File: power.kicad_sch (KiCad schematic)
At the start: 28 parts, among them U12 TPS54302, U2 SCT2450

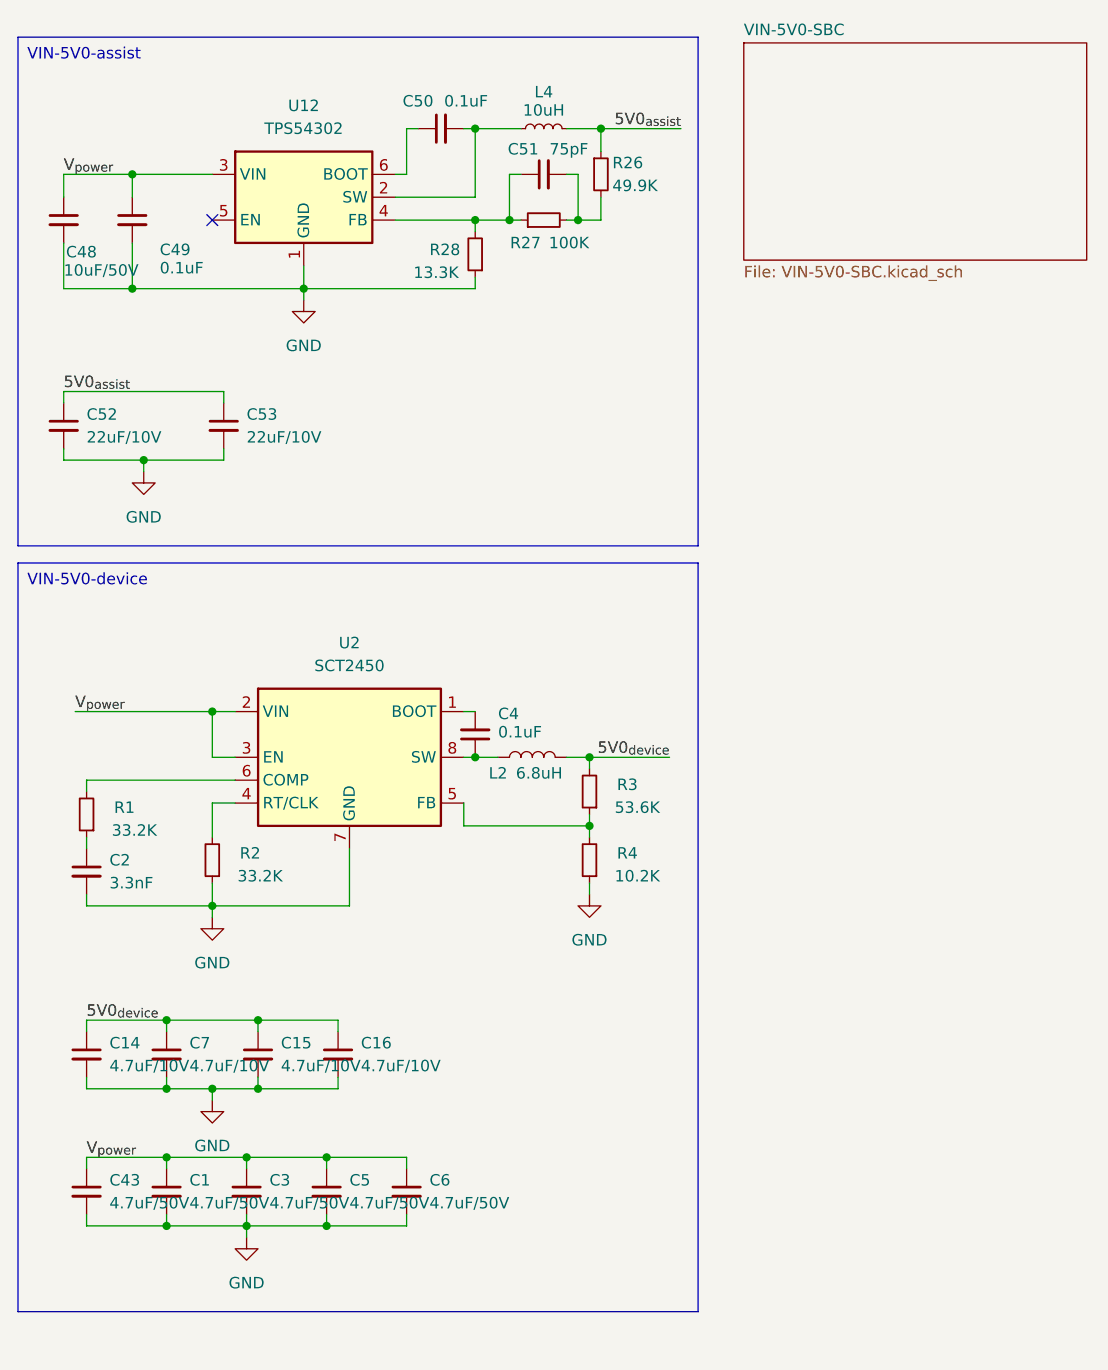
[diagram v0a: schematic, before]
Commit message: 暂存: 基本完成原理图(未分配封装，未ERC)
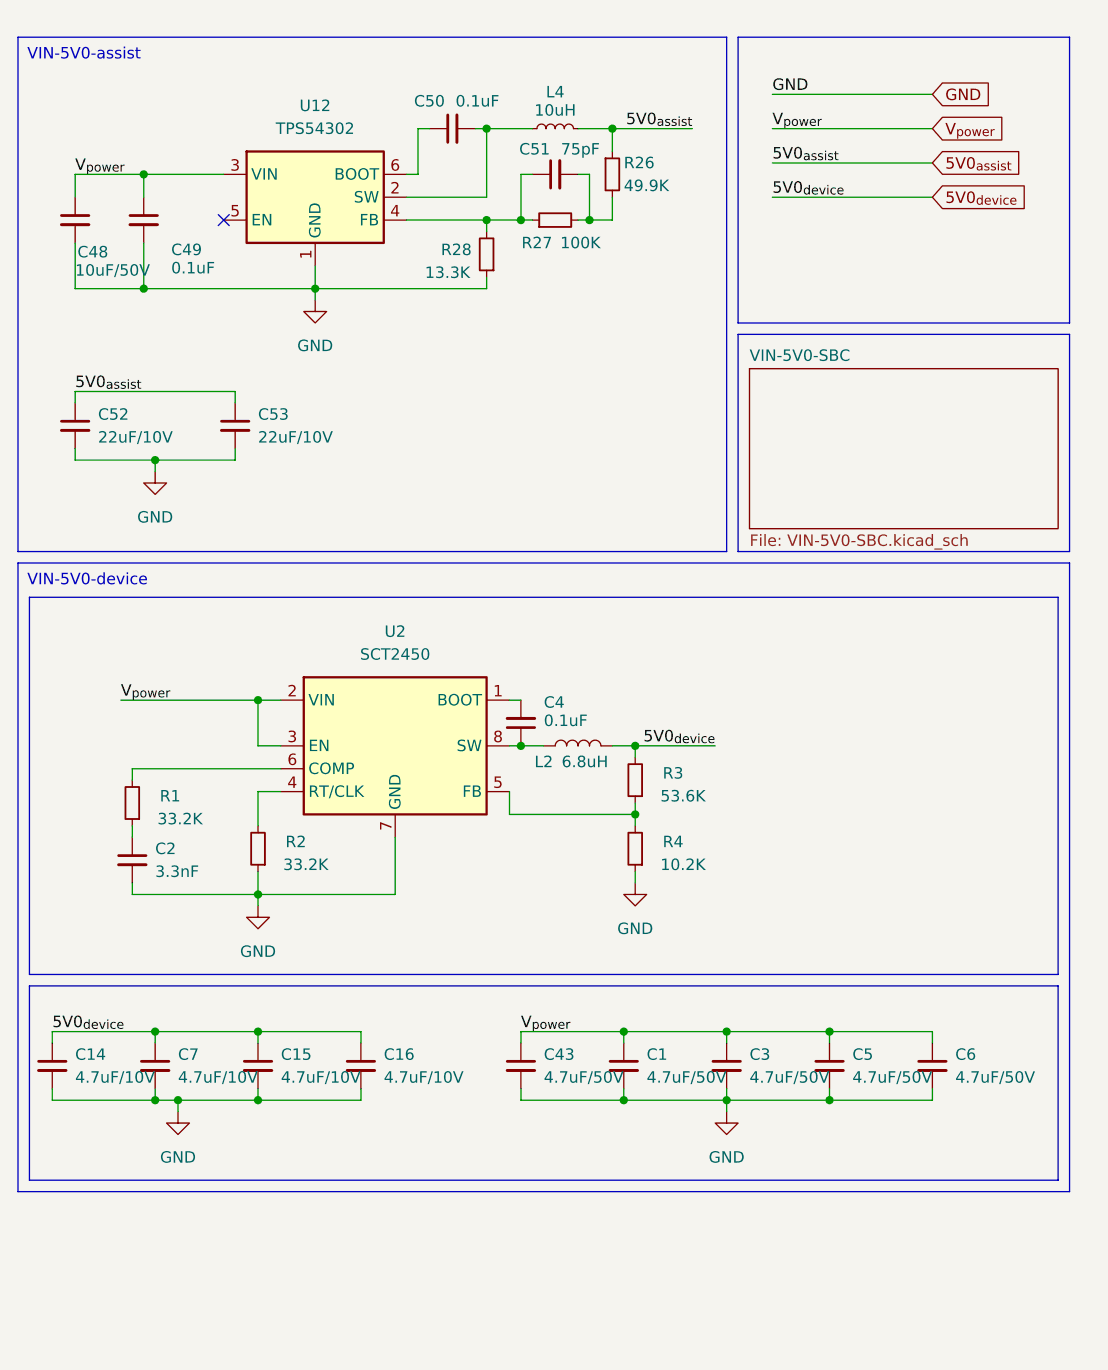
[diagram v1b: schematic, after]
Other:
- moved on the sheet: C1, C14, C15, C16, C2, C3, C4, C43, C48, C49, C5, C50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

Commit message: 暂存: 基本完成原理图(差雷达接口)
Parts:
- C12: renamed from C14; footprint (none) -> Capacitor_SMD:C_0603_1608Metric
- C13: renamed from C48; footprint (none) -> Capacitor_SMD:C_1206_3216Metric
- C14: renamed from C52; footprint (none) -> Capacitor_SMD:C_1206_3216Metric
- C15: renamed from C2; footprint (none) -> Capacitor_SMD:C_0402_1005Metric
- C16: renamed from C49; footprint (none) -> Capacitor_SMD:C_0402_1005Metric
- C17: renamed from C7; footprint (none) -> Capacitor_SMD:C_0603_1608Metric
- C18: renamed from C53; footprint (none) -> Capacitor_SMD:C_1206_3216Metric
- C19: renamed from C15; footprint (none) -> Capacitor_SMD:C_0603_1608Metric
- C20: renamed from C16; footprint (none) -> Capacitor_SMD:C_0603_1608Metric
- C21: renamed from C50; footprint (none) -> Capacitor_SMD:C_0402_1005Metric
- C22: renamed from C4; footprint (none) -> Capacitor_SMD:C_0402_1005Metric
- C23: renamed from C43; footprint (none) -> Capacitor_SMD:C_0805_2012Metric
- C24: renamed from C51; footprint (none) -> Capacitor_SMD:C_0402_1005Metric
- C25: renamed from C1; footprint (none) -> Capacitor_SMD:C_0805_2012Metric
- C26: renamed from C3; footprint (none) -> Capacitor_SMD:C_0805_2012Metric
- C27: renamed from C5; footprint (none) -> Capacitor_SMD:C_0805_2012Metric
- C28: renamed from C6; footprint (none) -> Capacitor_SMD:C_0805_2012Metric
- L1: renamed from L4; footprint (none) -> Inductor_SMD:L_APV_APH0530
- L2: footprint (none) -> Inductor_SMD:L_APV_APH0630
- R10: renamed from R27; footprint (none) -> Resistor_SMD:R_0402_1005Metric
- R11: renamed from R26; footprint (none) -> Resistor_SMD:R_0603_1608Metric
- R12: renamed from R3; footprint (none) -> Resistor_SMD:R_0603_1608Metric
- R13: renamed from R4; footprint (none) -> Resistor_SMD:R_0603_1608Metric
- R7: renamed from R1; footprint (none) -> Resistor_SMD:R_0603_1608Metric
- R8: renamed from R2; value 33.2K -> 200K; footprint (none) -> Resistor_SMD:R_0402_1005Metric
- R9: renamed from R28; footprint (none) -> Resistor_SMD:R_0603_1608Metric
- U5: renamed from U2; footprint (none) -> Package_SO:HSOP-8-1EP_3.9x4.9mm_P1.27mm_EP2.3x2.3mm
- renumbered U12 to U4

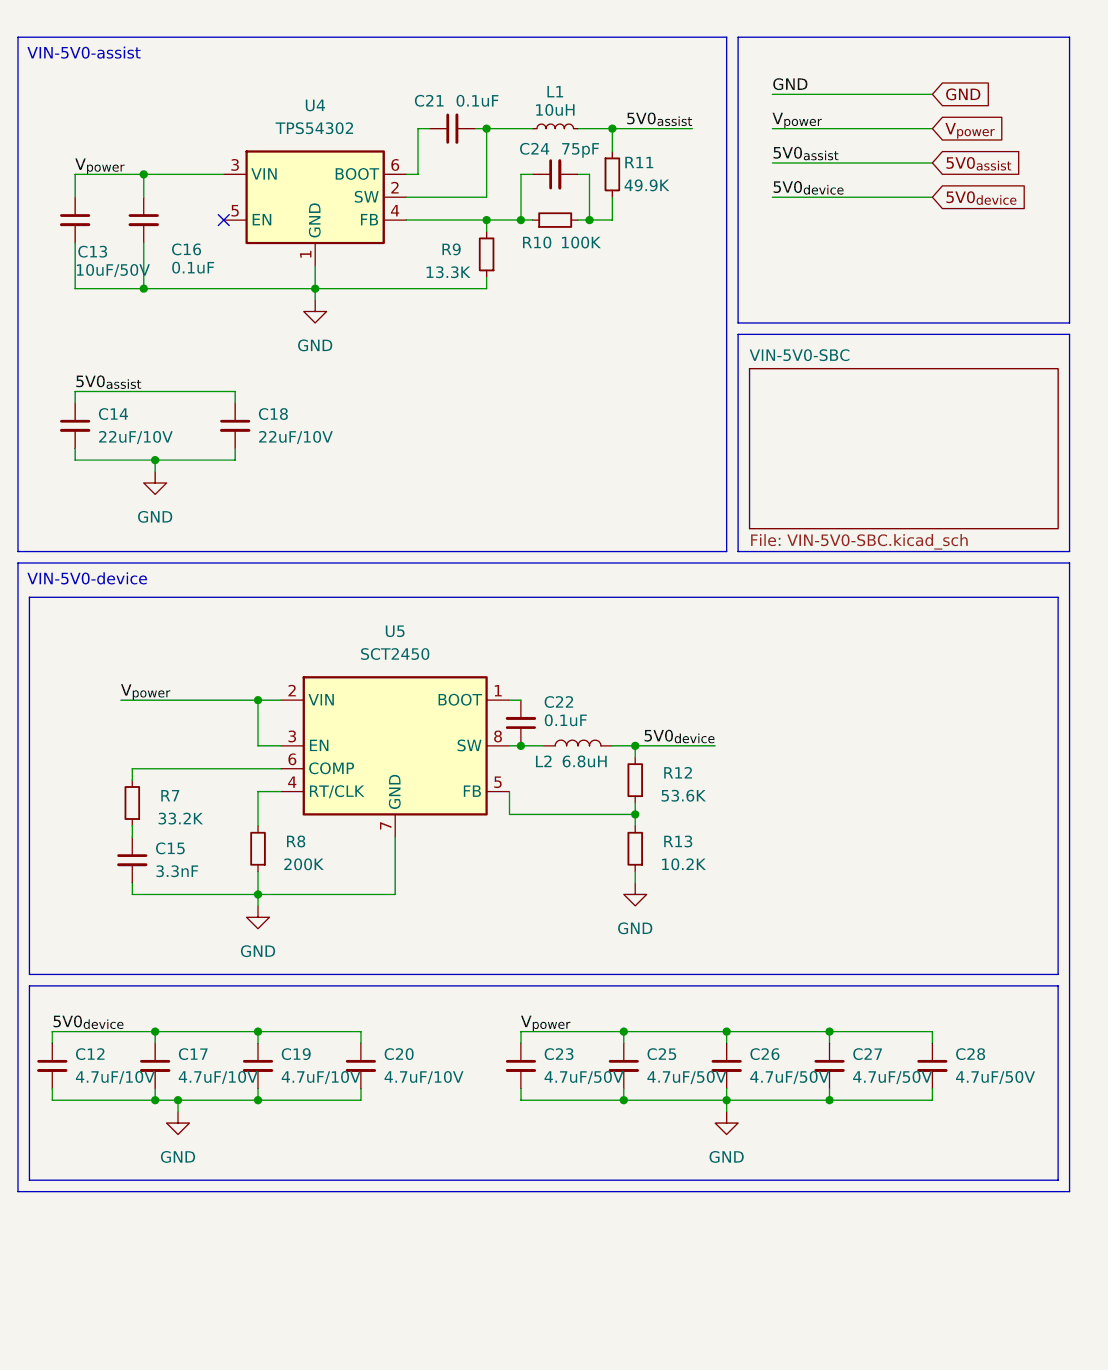
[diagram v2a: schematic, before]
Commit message: 暂存: 布局布线基本完成(DRC未过，GND不全)
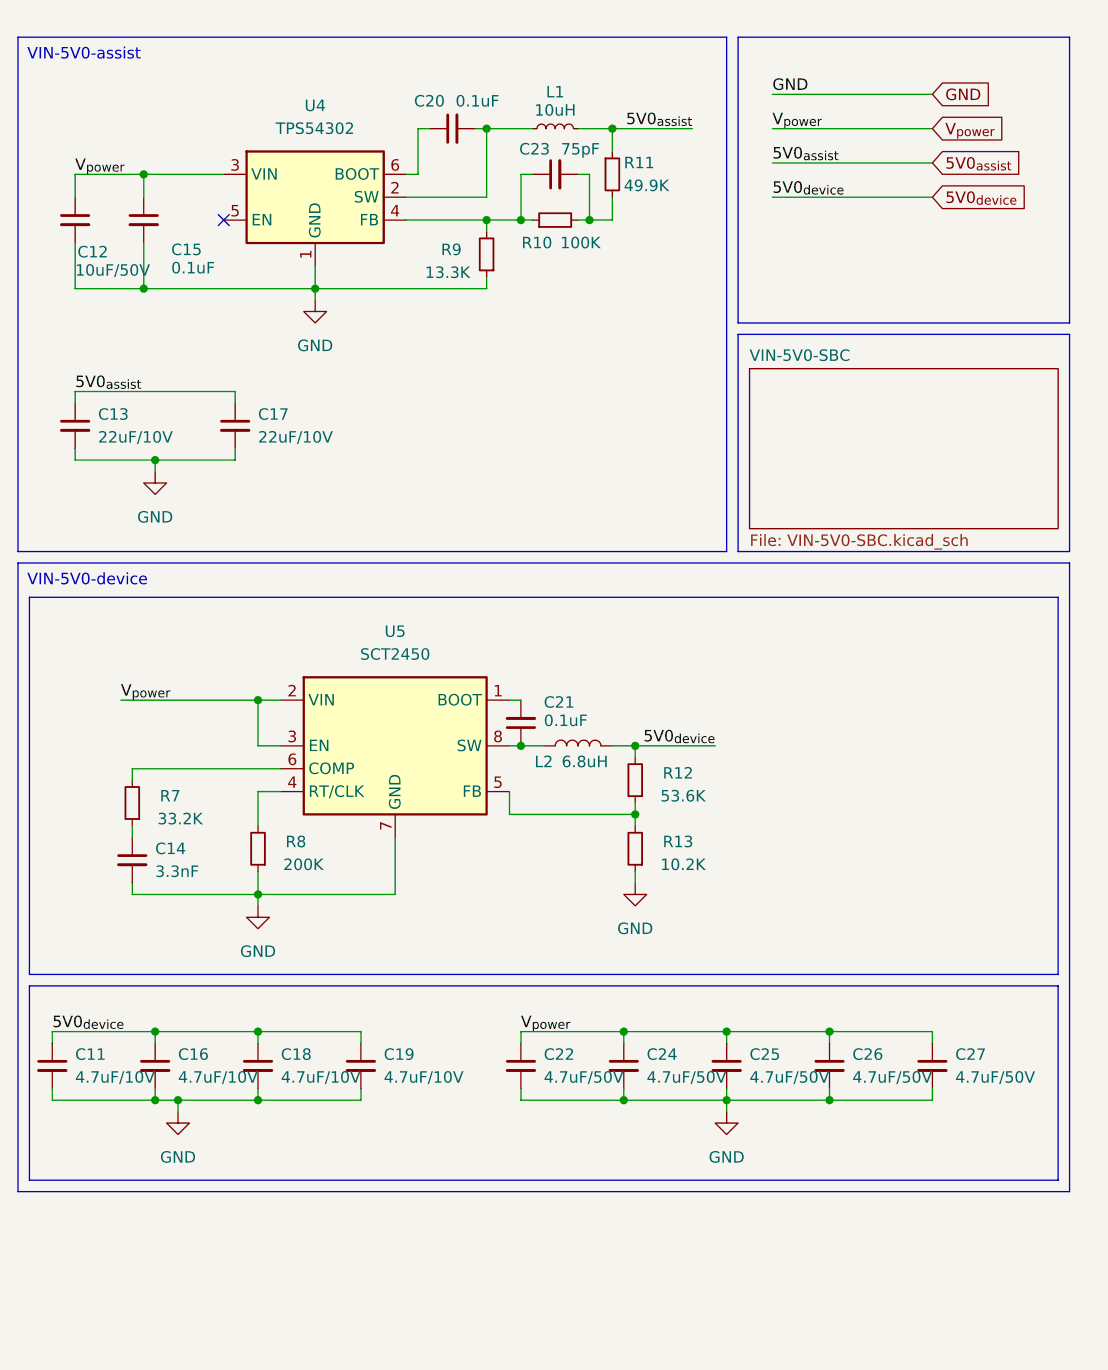
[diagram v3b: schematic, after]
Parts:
- renumbered C12 to C11, C13 to C12, C14 to C13, C15 to C14, C16 to C15, C17 to C16, C18 to C17, C19 to C18, C20 to C19, C21 to C20, C22 to C21, C23 to C22, C24 to C23, C25 to C24, C26 to C25, C27 to C26, C28 to C27
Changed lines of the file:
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@@
 		(on_board yes)
 		(dnp no)
-		(property "Reference" "C21"
+		(property "Reference" "C20"
 			(at 81.28 40.132 90)
 			(effects
@@
 			(project ""
 				(path "/c658c753-a869-4eb9-a520-6b2e7fae7fd9/9517e653-294f-4743-9b8d-25bbdad54970"
-					(reference "C21")
+					(reference "C20")
 					(unit 1)
 				)
@@
 		(dnp no)
 		(fields_autoplaced yes)
-		(property "Reference" "C19"
+		(property "Reference" "C18"
 			(at 64.77 146.0562 0)
 			(effects
@@
 			(project "ZW1S"
 				(path "/c658c753-a869-4eb9-a520-6b2e7fae7fd9/9517e653-294f-4743-9b8d-25bbdad54970"
-					(reference "C19")
+					(reference "C18")
 					(unit 1)
 				)
@@
 		(dnp no)
 		(fields_autoplaced yes)
-		(property "Reference" "C27"
+		(property "Reference" "C26"
 			(at 128.27 146.0562 0)
 			(effects
@@
 			(project "ZW1S"
 				(path "/c658c753-a869-4eb9-a520-6b2e7fae7fd9/9517e653-294f-4743-9b8d-25bbdad54970"
-					(reference "C27")
+					(reference "C26")
 					(unit 1)
 				)
@@
 		(dnp no)
 		(fields_autoplaced yes)
-		(property "Reference" "C17"
+		(property "Reference" "C16"
 			(at 53.34 146.0562 0)
 			(effects
@@
 			(project "ZW1S"
 				(path "/c658c753-a869-4eb9-a520-6b2e7fae7fd9/9517e653-294f-4743-9b8d-25bbdad54970"
-					(reference "C17")
+					(reference "C16")
 					(unit 1)
 				)
@@
 		(dnp no)
 		(fields_autoplaced yes)
-		(property "Reference" "C15"
+		(property "Reference" "C14"
 			(at 50.8 123.1962 0)
 			(effects
@@
 			(project ""
 				(path "/c658c753-a869-4eb9-a520-6b2e7fae7fd9/9517e653-294f-4743-9b8d-25bbdad54970"
-					(reference "C15")
+					(reference "C14")
 					(unit 1)
 				)
@@
 		(dnp no)
 		(fields_autoplaced yes)
-		(property "Reference" "C26"
+		(property "Reference" "C25"
 			(at 116.84 146.0562 0)
 			(effects
@@
 			(project "ZW1S"
 				(path "/c658c753-a869-4eb9-a520-6b2e7fae7fd9/9517e653-294f-4743-9b8d-25bbdad54970"
-					(reference "C26")
+					(reference "C25")
 					(unit 1)
 				)
@@
 		(dnp no)
 		(fields_autoplaced yes)
-		(property "Reference" "C25"
+		(property "Reference" "C24"
 			(at 105.41 146.0562 0)
 			(effects
@@
 			(project "ZW1S"
 				(path "/c658c753-a869-4eb9-a520-6b2e7fae7fd9/9517e653-294f-4743-9b8d-25bbdad54970"
-					(reference "C25")
+					(reference "C24")
 					(unit 1)
 				)
@@
 		(dnp no)
 		(fields_autoplaced yes)
-		(property "Reference" "C28"
+		(property "Reference" "C27"
 			(at 139.7 146.0562 0)
 			(effects
@@
 			(project "ZW1S"
 				(path "/c658c753-a869-4eb9-a520-6b2e7fae7fd9/9517e653-294f-4743-9b8d-25bbdad54970"
-					(reference "C28")
+					(reference "C27")
 					(unit 1)
 				)
@@
 		(dnp no)
 		(fields_autoplaced yes)
-		(property "Reference" "C23"
+		(property "Reference" "C22"
 			(at 93.98 146.0562 0)
 			(effects
@@
 			(project ""
 				(path "/c658c753-a869-4eb9-a520-6b2e7fae7fd9/9517e653-294f-4743-9b8d-25bbdad54970"
-					(reference "C23")
+					(reference "C22")
 					(unit 1)
 				)
@@
 		(dnp no)
 		(fields_autoplaced yes)
-		(property "Reference" "C18"
+		(property "Reference" "C17"
 			(at 62.23 74.9362 0)
 			(effects
@@
 			(project "ZW1S"
 				(path "/c658c753-a869-4eb9-a520-6b2e7fae7fd9/9517e653-294f-4743-9b8d-25bbdad54970"
-					(reference "C18")
+					(reference "C17")
 					(unit 1)
 				)
@@
 		(on_board yes)
 		(dnp no)
-		(property "Reference" "C22"
+		(property "Reference" "C21"
 			(at 93.98 106.934 0)
 			(effects
@@
 			(project "ZW1S"
 				(path "/c658c753-a869-4eb9-a520-6b2e7fae7fd9/9517e653-294f-4743-9b8d-25bbdad54970"
-					(reference "C22")
+					(reference "C21")
 					(unit 1)
 				)
@@
 		(dnp no)
 		(fields_autoplaced yes)
-		(property "Reference" "C14"
+		(property "Reference" "C13"
 			(at 44.45 74.9362 0)
 			(effects
@@
 			(project "ZW1S"
 				(path "/c658c753-a869-4eb9-a520-6b2e7fae7fd9/9517e653-294f-4743-9b8d-25bbdad54970"
-					(reference "C14")
+					(reference "C13")
 					(unit 1)
 				)
@@
 		(on_board yes)
 		(dnp no)
-		(property "Reference" "C16"
+		(property "Reference" "C15"
 			(at 52.578 56.642 0)
 			(effects
@@
 			(project "ZW1S"
 				(path "/c658c753-a869-4eb9-a520-6b2e7fae7fd9/9517e653-294f-4743-9b8d-25bbdad54970"
-					(reference "C16")
+					(reference "C15")
 					(unit 1)
 				)
@@
 		(on_board yes)
 		(dnp no)
-		(property "Reference" "C13"
+		(property "Reference" "C12"
 			(at 42.164 56.896 0)
 			(effects
@@
 			(project ""
 				(path "/c658c753-a869-4eb9-a520-6b2e7fae7fd9/9517e653-294f-4743-9b8d-25bbdad54970"
-					(reference "C13")
+					(reference "C12")
 					(unit 1)
 				)
@@
 		(on_board yes)
 		(dnp no)
-		(property "Reference" "C24"
+		(property "Reference" "C23"
 			(at 92.964 45.466 90)
 			(effects
@@
 			(project ""
 				(path "/c658c753-a869-4eb9-a520-6b2e7fae7fd9/9517e653-294f-4743-9b8d-25bbdad54970"
-					(reference "C24")
+					(reference "C23")
 					(unit 1)
 				)
@@
 		(dnp no)
 		(fields_autoplaced yes)
-		(property "Reference" "C12"
+		(property "Reference" "C11"
 			(at 41.91 146.0562 0)
 			(effects
@@
 			(project "ZW1S"
 				(path "/c658c753-a869-4eb9-a520-6b2e7fae7fd9/9517e653-294f-4743-9b8d-25bbdad54970"
-					(reference "C12")
+					(reference "C11")
 					(unit 1)
 				)
@@
 		(dnp no)
 		(fields_autoplaced yes)
-		(property "Reference" "C20"
+		(property "Reference" "C19"
 			(at 76.2 146.0562 0)
 			(effects
@@
 			(project "ZW1S"
 				(path "/c658c753-a869-4eb9-a520-6b2e7fae7fd9/9517e653-294f-4743-9b8d-25bbdad54970"
-					(reference "C20")
-					(unit 1)
-				)
+					(reference "C19")
+					(unit 1)
+				)

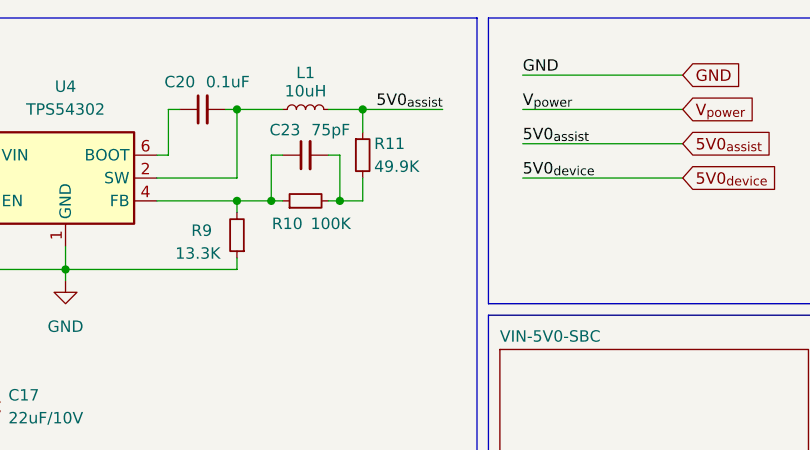
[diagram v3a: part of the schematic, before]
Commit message: fix: 修正TPS54302反馈电阻值
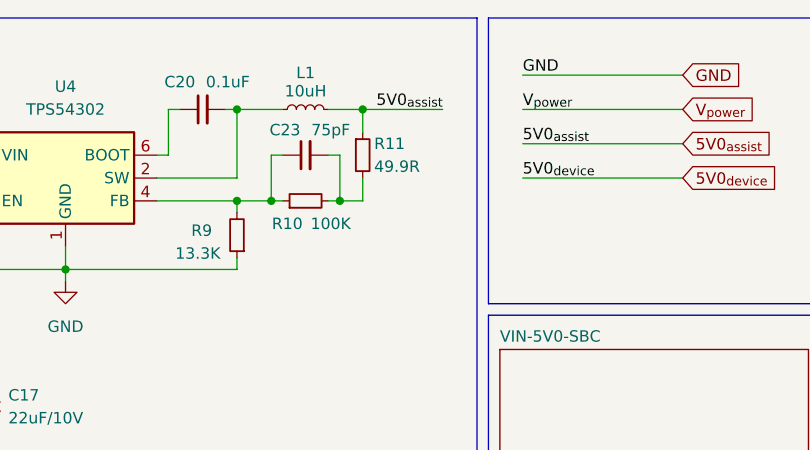
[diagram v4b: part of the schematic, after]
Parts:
- R11: value 49.9K -> 49.9R
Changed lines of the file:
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@@
 			)
 		)
-		(property "Value" "49.9K"
+		(property "Value" "49.9R"
 			(at 102.87 49.53 0)
 			(effects
